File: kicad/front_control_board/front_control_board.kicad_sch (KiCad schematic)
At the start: 8 parts

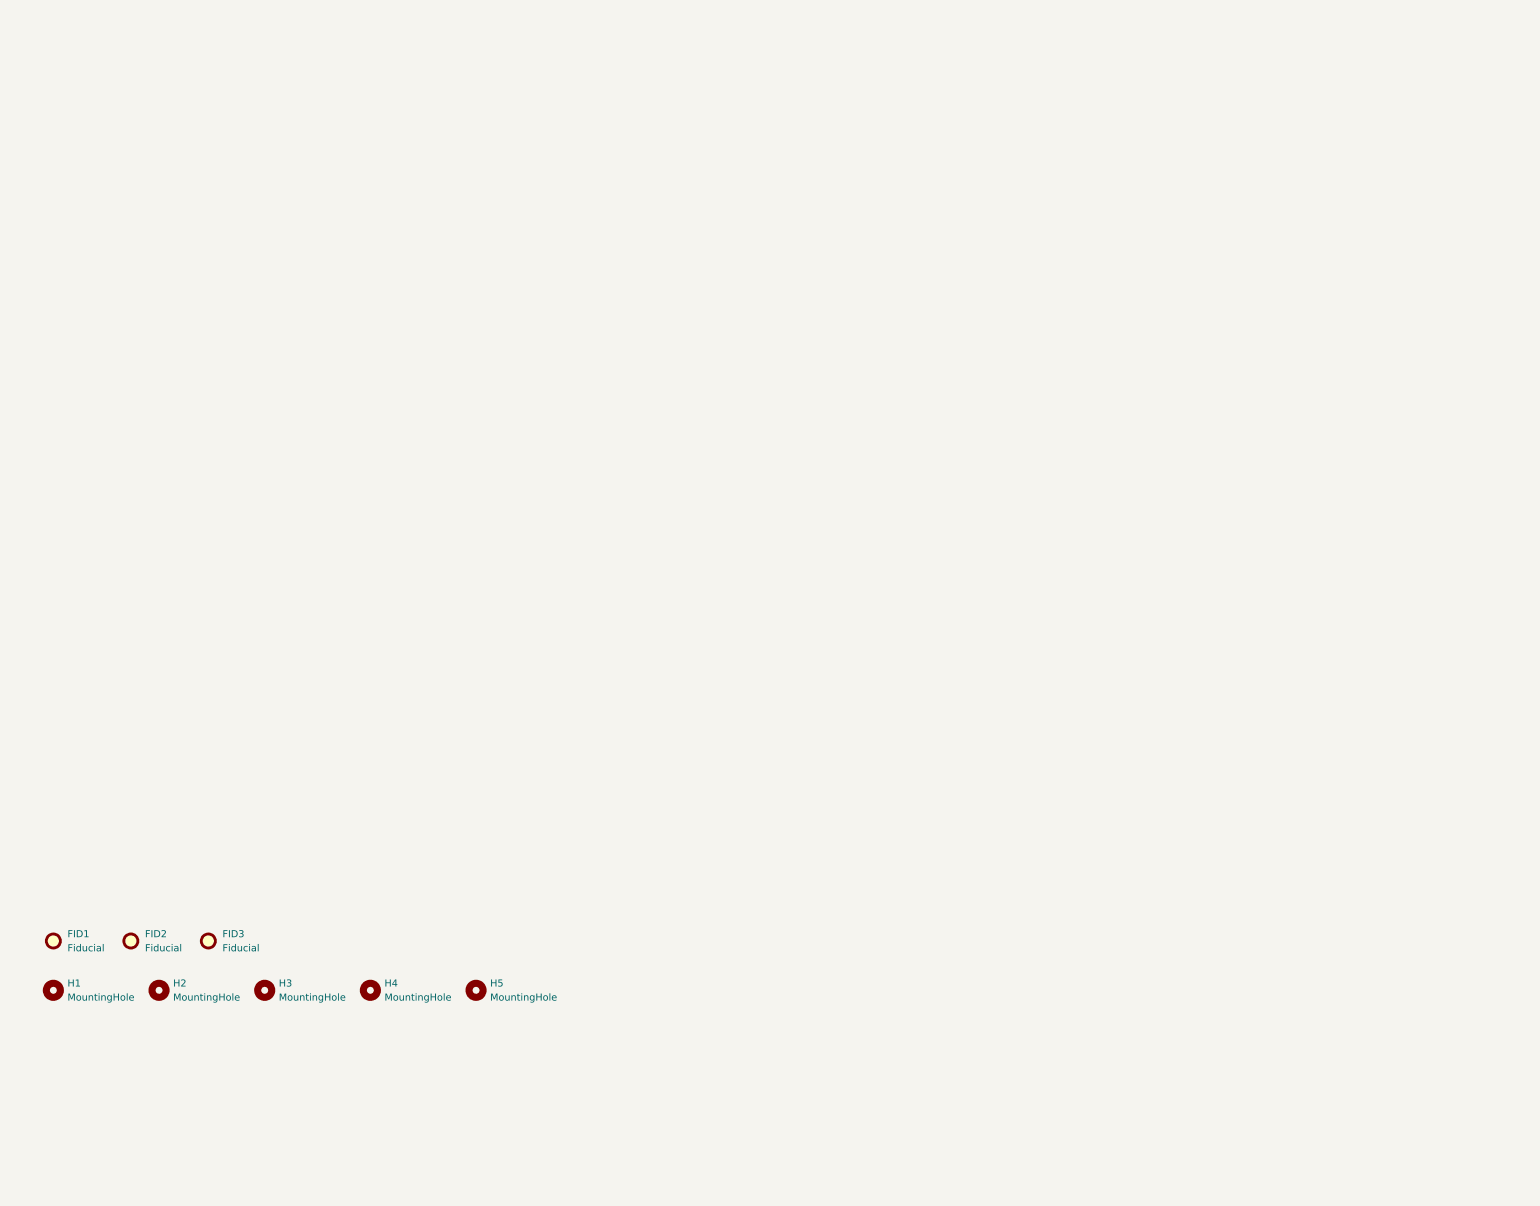
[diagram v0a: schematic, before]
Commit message: add front panel control
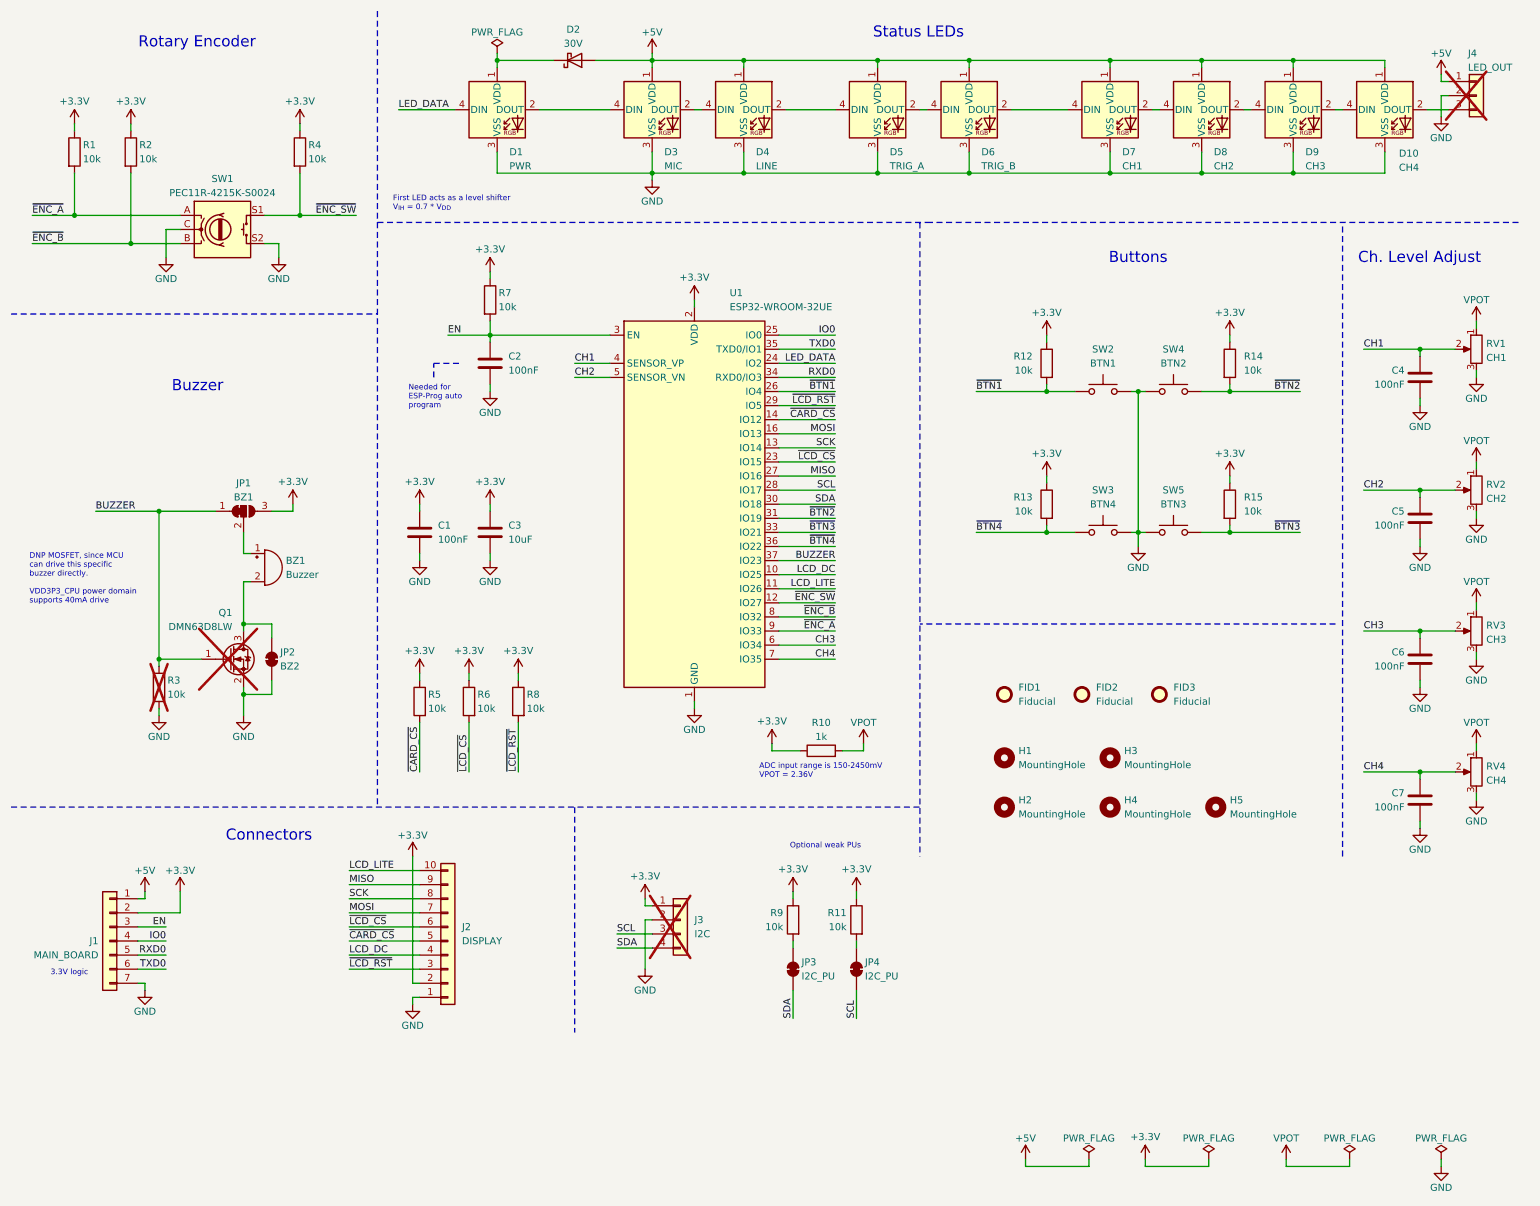
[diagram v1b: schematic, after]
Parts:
- added BZ1: Buzzer, Buzzer_Beeper:Buzzer_12x9.5RM7.6, symbol Device:Buzzer
- added C1, C2, C4, C5, C6, C7: 100nF, Capacitor_SMD:C_0603_1608Metric, symbol Device:C
- added C3: 10uF, Capacitor_SMD:C_0603_1608Metric, symbol Device:C
- added D1: PWR, LED_SMD:LED_WS2812B_PLCC4_5.0x5.0mm_P3.2mm, symbol LED:WS2812B
- added D10: CH4, LED_SMD:LED_WS2812B_PLCC4_5.0x5.0mm_P3.2mm, symbol LED:WS2812B
- added D2: 30V, Diode_SMD:D_SOD-523, symbol Device:D_Schottky
- added D3: MIC, LED_SMD:LED_WS2812B_PLCC4_5.0x5.0mm_P3.2mm, symbol LED:WS2812B
- added D4: LINE, LED_SMD:LED_WS2812B_PLCC4_5.0x5.0mm_P3.2mm, symbol LED:WS2812B
- added D5: TRIG_A, LED_SMD:LED_WS2812B_PLCC4_5.0x5.0mm_P3.2mm, symbol LED:WS2812B
- added D6: TRIG_B, LED_SMD:LED_WS2812B_PLCC4_5.0x5.0mm_P3.2mm, symbol LED:WS2812B
- added D7: CH1, LED_SMD:LED_WS2812B_PLCC4_5.0x5.0mm_P3.2mm, symbol LED:WS2812B
- added D8: CH2, LED_SMD:LED_WS2812B_PLCC4_5.0x5.0mm_P3.2mm, symbol LED:WS2812B
- added D9: CH3, LED_SMD:LED_WS2812B_PLCC4_5.0x5.0mm_P3.2mm, symbol LED:WS2812B
- added J1: MAIN_BOARD, Connector_JST:JST_PH_B8B-PH-K_1x07_P2.00mm_Vertical, symbol Connector_Generic:Conn_01x07
- added J2: DISPLAY, Connector_PinHeader_2.54mm:PinHeader_1x10_P2.54mm_Vertical, symbol Connector_Generic:Conn_01x10
- added J3: I2C, Connector_PinHeader_2.54mm:PinHeader_1x04_P2.54mm_Vertical, symbol Connector_Generic:Conn_01x04
- added J4: LED_OUT, Connector_PinHeader_2.54mm:PinHeader_1x03_P2.54mm_Vertical, symbol Connector_Generic:Conn_01x03
- added JP1: BZ1, Jumper:SolderJumper-3_P1.3mm_Bridged12_RoundedPad1.0x1.5mm_NumberLabels, symbol Jumper:SolderJumper_3_Bridged12
- added JP2: BZ2, Jumper:SolderJumper-2_P1.3mm_Bridged_RoundedPad1.0x1.5mm, symbol Jumper:SolderJumper_2_Bridged
- added JP3, JP4: I2C_PU, Jumper:SolderJumper-2_P1.3mm_Bridged_RoundedPad1.0x1.5mm, symbol Jumper:SolderJumper_2_Bridged
- added Q1: DMN63D8LW, Package_TO_SOT_SMD:SOT-323_SC-70, symbol Device:Q_NMOS_GSD
- added R1, R11, R12, R13, R14, R15, R2, R3, R4, R5, R6, R7, R8, R9: 10k, Resistor_SMD:R_0603_1608Metric, symbol Device:R
- added R10: 1k, Resistor_SMD:R_0603_1608Metric, symbol Device:R
- added RV1: CH1, Potentiometer_THT:Potentiometer_Bourns_PTV09A-1_Single_Vertical, symbol Device:R_Potentiometer
- added RV2: CH2, Potentiometer_THT:Potentiometer_Bourns_PTV09A-1_Single_Vertical, symbol Device:R_Potentiometer
- added RV3: CH3, Potentiometer_THT:Potentiometer_Bourns_PTV09A-1_Single_Vertical, symbol Device:R_Potentiometer
- added RV4: CH4, Potentiometer_THT:Potentiometer_Bourns_PTV09A-1_Single_Vertical, symbol Device:R_Potentiometer
- added SW1: PEC11R-4215K-S0024, SaawLib:Rotary_Encoder_Switched_PEC11R, symbol Device:RotaryEncoder_Switch
- added SW2: BTN1, SaawLib:D6C, symbol Switch:SW_Push
- added SW3: BTN4, SaawLib:D6C, symbol Switch:SW_Push
- added SW4: BTN2, SaawLib:D6C, symbol Switch:SW_Push
- added SW5: BTN3, SaawLib:D6C, symbol Switch:SW_Push
- added U1: ESP32-WROOM-32UE, RF_Module:ESP32-WROOM-32UE, symbol RF_Module:ESP32-WROOM-32UE
- renumbered H3 to H2, H2 to H3
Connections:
- new net: D6.2 (DOUT), D7.4 (DIN)
- new net: D5.2 (DOUT), D6.4 (DIN)
- new net: D10.4 (DIN), D9.2 (DOUT)
- new net: D8.2 (DOUT), D9.4 (DIN)
- new net: D1.1 (VDD), D2.1 (K)
- new net: D1.2 (DOUT), D3.4 (DIN)
- new net: D7.2 (DOUT), D8.4 (DIN)
- new net: D10.2 (DOUT), J4.3 (Pin_3)
- new net: D4.2 (DOUT), D5.4 (DIN)
- new net: D3.2 (DOUT), D4.4 (DIN)
- new net: BZ1.2 (-), JP2.2 (B), Q1.3 (D)
- new net: JP3.2 (B), R9.2
- new net: JP4.2 (B), R11.2
- new net: BZ1.1 (+), JP1.2 (C)
- new net +3.3V: C1.1, C3.1, J1.2 (Pin_2), J2.2 (Pin_2), J3.1 (Pin_1), JP1.3 (B), R1.1, R10.1, R11.1, R12.1, R13.1, R14.1, R15.1, R2.1, R4.1, R5.1, R6.1, R7.1, R8.1, R9.1, U1.2 (VDD)
- new net +5V: D10.1 (VDD), D2.2 (A), D3.1 (VDD), D4.1 (VDD), D5.1 (VDD), D6.1 (VDD), D7.1 (VDD), D8.1 (VDD), D9.1 (VDD), J1.1 (Pin_1), J4.1 (Pin_1)
- new net BUZZER: JP1.1 (A), Q1.1 (G), R3.2, U1.37 (IO23)
- new net CH1: C4.1, RV1.2, U1.4 (SENSOR_VP)
- new net CH2: C5.1, RV2.2, U1.5 (SENSOR_VN)
- new net CH3: C6.1, RV3.2, U1.6 (IO34)
- new net CH4: C7.1, RV4.2, U1.7 (IO35)
- new net EN: C2.1, J1.3 (Pin_3), R7.2, U1.3 (EN)
- new net GND: C1.2, C2.2, C3.2, C4.2, C5.2, C6.2, C7.2, D1.3 (VSS), D10.3 (VSS), D3.3 (VSS), D4.3 (VSS), D5.3 (VSS), D6.3 (VSS), D7.3 (VSS), D8.3 (VSS), D9.3 (VSS), J1.7 (Pin_7), J2.1 (Pin_1), J3.2 (Pin_2), J4.2 (Pin_2), JP2.1 (A), Q1.2 (S), R3.1, RV1.3, RV2.3, RV3.3, RV4.3, SW1.C, SW1.S2, SW2.1, SW3.1, SW4.1, SW5.1, U1.1 (GND), U1.15 (GND), U1.38 (GND), U1.39 (GND)
- new net IO0: J1.4 (Pin_4), U1.25 (IO0)
- new net LCD_DC: J2.4 (Pin_4), U1.10 (IO25)
- new net LCD_LITE: J2.10 (Pin_10), U1.11 (IO26)
- new net LED_DATA: D1.4 (DIN), U1.24 (IO2)
- new net MISO: J2.9 (Pin_9), U1.27 (IO16)
- new net MOSI: J2.7 (Pin_7), U1.16 (IO13)
- new net RXD0: J1.5 (Pin_5), U1.34 (RXD0/IO3)
- new net SCK: J2.8 (Pin_8), U1.13 (IO14)
- new net SCL: J3.3 (Pin_3), JP4.1 (A), U1.28 (IO17)
- new net SDA: J3.4 (Pin_4), JP3.1 (A), U1.30 (IO18)
- new net TXD0: J1.6 (Pin_6), U1.35 (TXD0/IO1)
- new net VPOT: R10.2, RV1.1, RV2.1, RV3.1, RV4.1
- new net ~{BTN1}: R12.2, SW2.2, U1.26 (IO4)
- new net ~{BTN2}: R14.2, SW4.2, U1.31 (IO19)
- new net ~{BTN3}: R15.2, SW5.2, U1.33 (IO21)
- new net ~{BTN4}: R13.2, SW3.2, U1.36 (IO22)
- new net ~{CARD_CS}: J2.5 (Pin_5), R5.2, U1.14 (IO12)
- new net ~{ENC_A}: R1.2, SW1.A, U1.9 (IO33)
- new net ~{ENC_B}: R2.2, SW1.B, U1.8 (IO32)
- new net ~{ENC_SW}: R4.2, SW1.S1, U1.12 (IO27)
- new net ~{LCD_CS}: J2.6 (Pin_6), R6.2, U1.23 (IO15)
- new net ~{LCD_RST}: J2.3 (Pin_3), R8.2, U1.29 (IO5)
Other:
- note added: "3.3V logic"
- note added: "ADC input range is 150-2450mV VPOT = 2.36V"
- note added: "Buttons"
- note added: "Buzzer"
- note added: "Ch. Level Adjust"
- note added: "Connectors"
- note added: "DNP MOSFET, since MCU can drive this specific buzzer directly. VDD3P3_CPU power domain supports 40mA drive"
- note added: "First LED acts as a level shifter V_{IH} = 0.7 * V_{DD}"
- note added: "Needed for ESP-Prog auto program"
- note added: "Optional weak PUs"
- note added: "Rotary Encoder"
- note added: "Status LEDs"
- moved on the sheet: FID1, FID2, FID3, H1, H2, H3, H4, H5

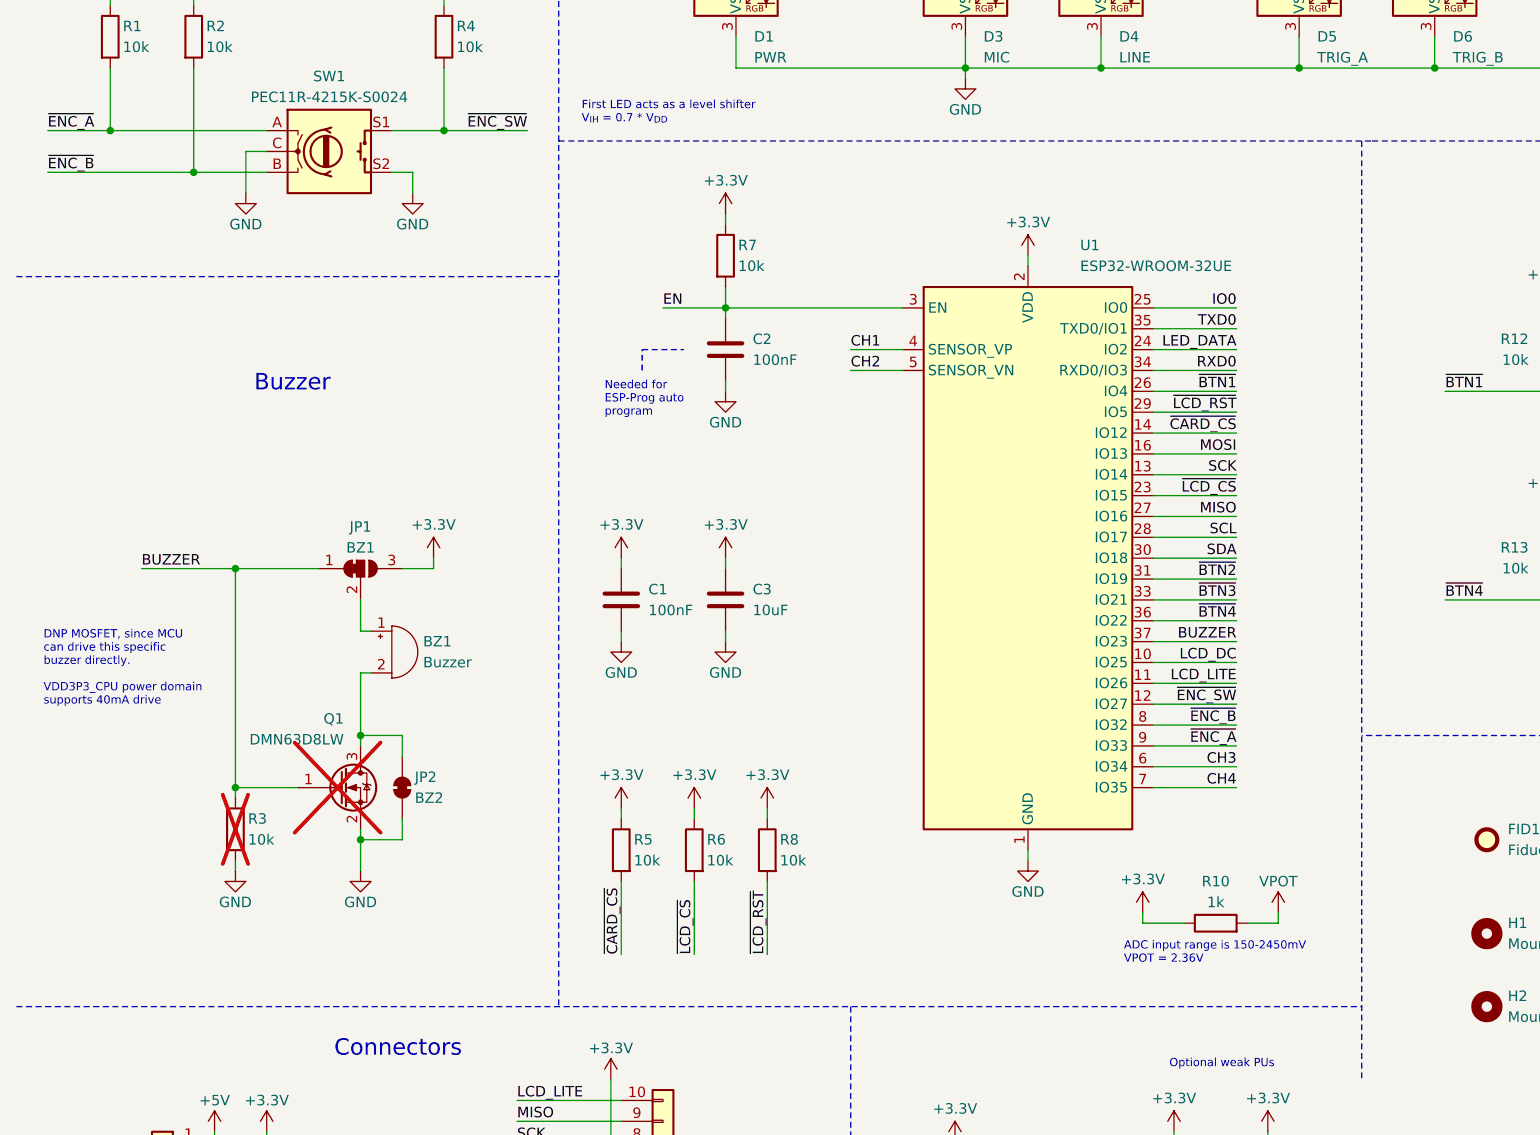
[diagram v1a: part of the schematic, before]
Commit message: reorder pins to use IO_MUX SPI
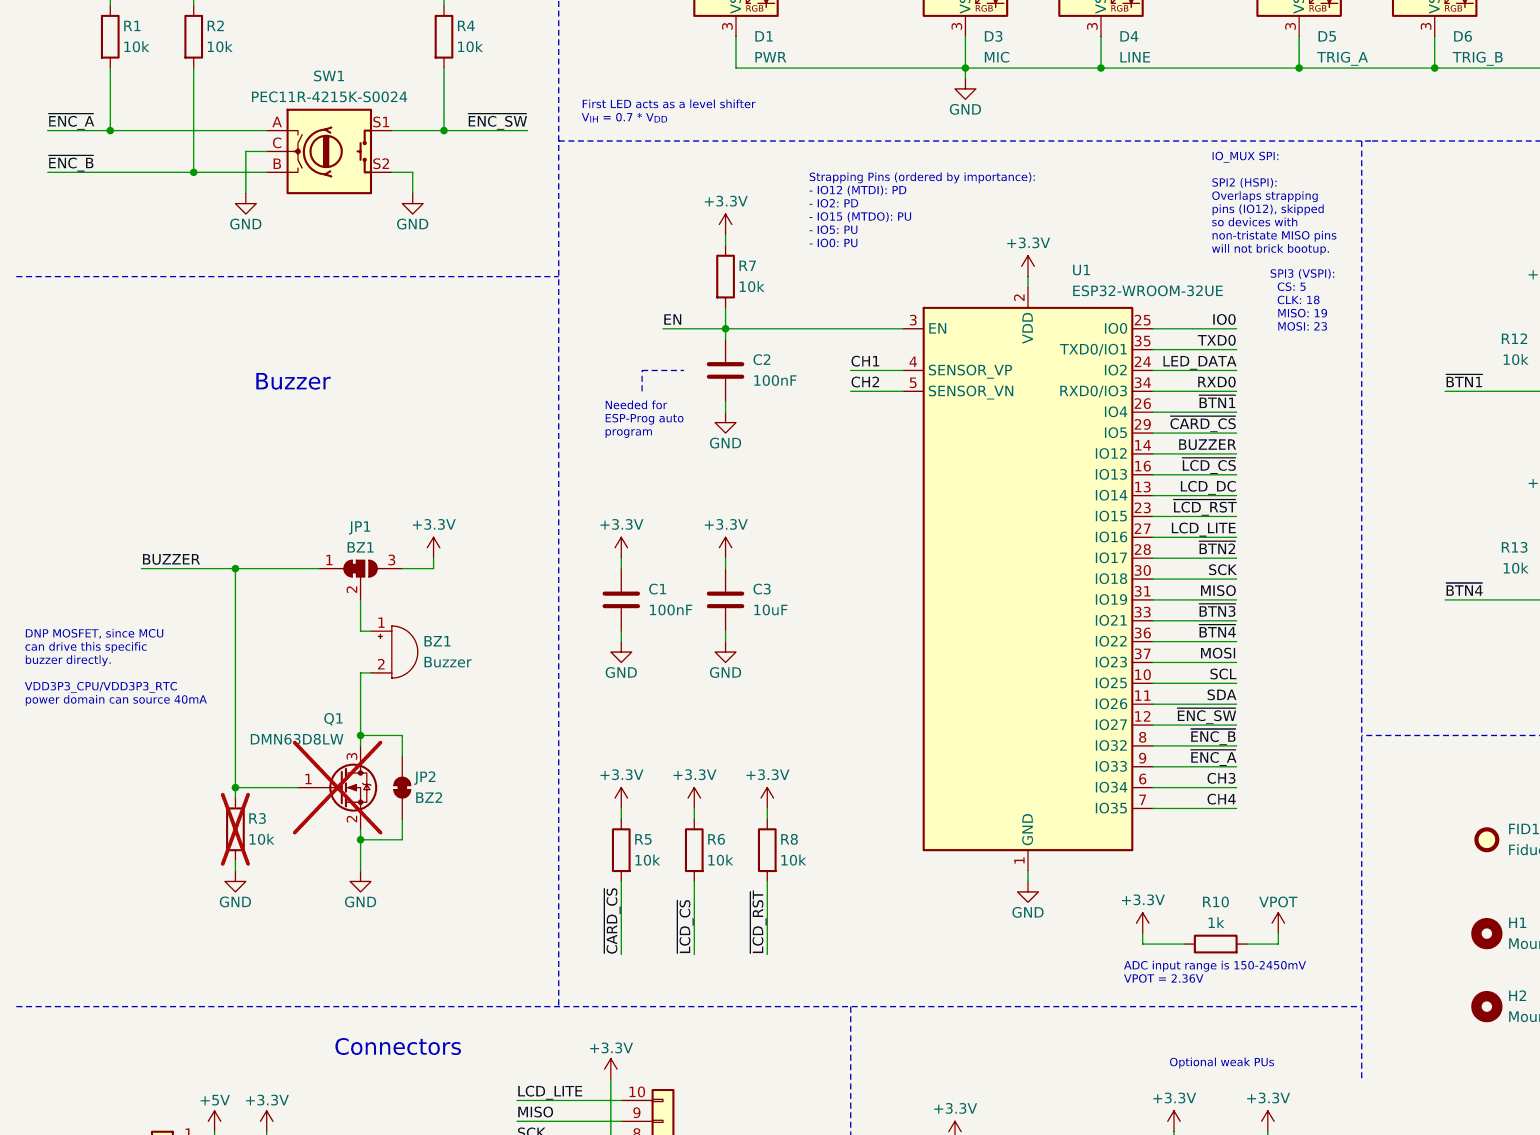
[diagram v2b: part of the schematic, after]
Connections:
- net BUZZER: now also U1.14 (IO12); no longer U1.37 (IO23)
- net LCD_DC: now also U1.13 (IO14); no longer U1.10 (IO25)
- net LCD_LITE: now also U1.27 (IO16); no longer U1.11 (IO26)
- net MISO: now also U1.31 (IO19); no longer U1.27 (IO16)
- net MOSI: now also U1.37 (IO23); no longer U1.16 (IO13)
- net SCK: now also U1.30 (IO18); no longer U1.13 (IO14)
- net SCL: now also U1.10 (IO25); no longer U1.28 (IO17)
- net SDA: now also U1.11 (IO26); no longer U1.30 (IO18)
- net ~{BTN2}: now also U1.28 (IO17); no longer U1.31 (IO19)
- net ~{CARD_CS}: now also U1.29 (IO5); no longer U1.14 (IO12)
- net ~{LCD_CS}: now also U1.16 (IO13); no longer U1.23 (IO15)
- net ~{LCD_RST}: now also U1.23 (IO15); no longer U1.29 (IO5)
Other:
- note added: "DNP MOSFET, since MCU can drive this specific buzzer directly. VDD3P3_CPU/VDD3P3_RTC power domain can source 40mA"
- note added: "IO_MUX SPI: SPI2 (HSPI): Overlaps strapping pins (IO12), skipped so devices with non-tristate MISO pins will not brick bootup."
- note added: "SPI3 (VSPI): CS: 5 CLK: 18 MISO: 19 MOSI: 23"
- note added: "Strapping Pins (ordered by importance): - IO12 (MTDI): PD - IO2: PD - IO15 (MTDO): PU - IO5: PU - IO0: PU"
- note removed: "DNP MOSFET, since MCU can drive this specific buzzer directly. VDD3P3_CPU power domain supports 40mA drive"
- moved on the sheet: C2, R10, R7, U1
